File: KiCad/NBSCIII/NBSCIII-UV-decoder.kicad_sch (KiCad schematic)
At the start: 29 parts, among them U2 4053, U3 LM324N

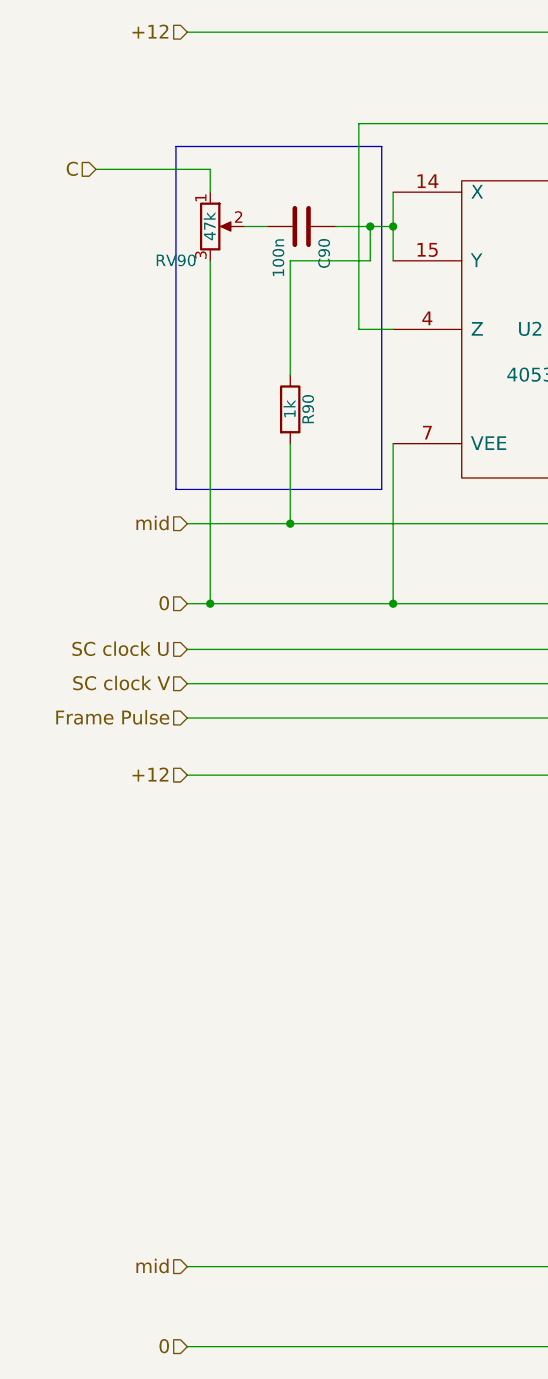
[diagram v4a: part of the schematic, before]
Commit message: Simplify power distribution and make global
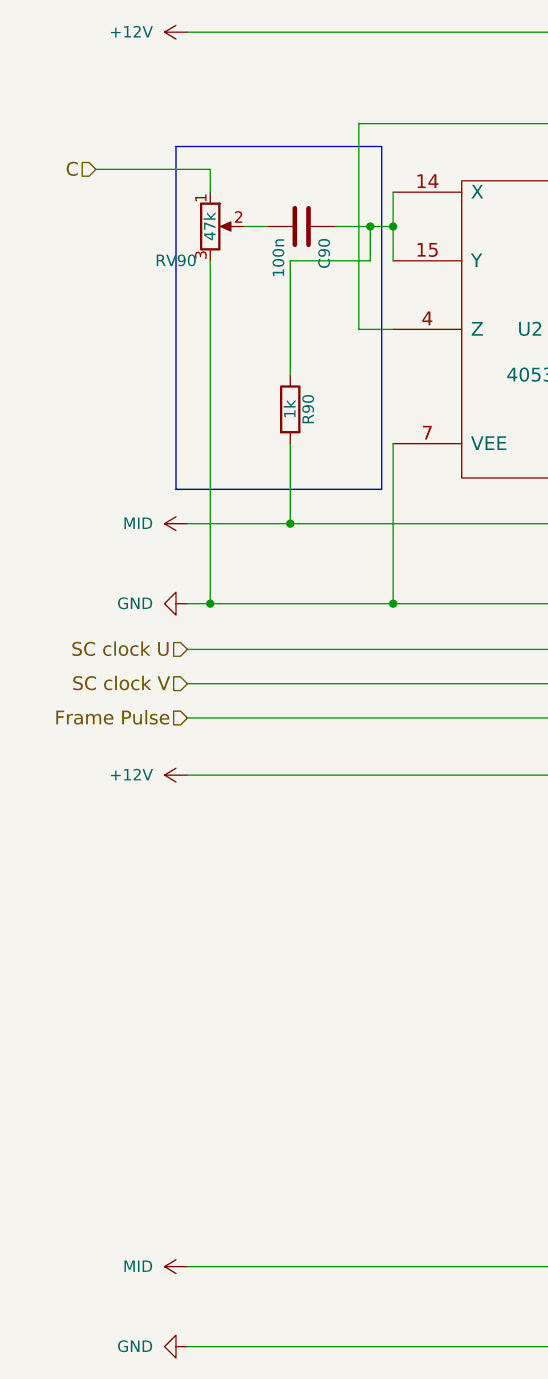
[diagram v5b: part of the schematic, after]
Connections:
- net VDD renamed +12V
- net VSS renamed GND
- net mid renamed MID
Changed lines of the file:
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@@
     (effects (font (size 1.524 1.524)) (justify left))
-  )
-  (hierarchical_label "mid" (shape input) (at 34.29 161.29 180)
-    (effects (font (size 1.524 1.524)) (justify right))
-  )
-  (hierarchical_label "mid" (shape input) (at 34.29 78.74 180)
-    (effects (font (size 1.524 1.524)) (justify right))
-  )
-  (hierarchical_label "+12" (shape input) (at 34.29 24.13 180)
-    (effects (font (size 1.524 1.524)) (justify right))
-  )
-  (hierarchical_label "+12" (shape input) (at 34.29 106.68 180)
-    (effects (font (size 1.524 1.524)) (justify right))
-  )
-  (hierarchical_label "0" (shape input) (at 34.29 87.63 180)
-    (effects (font (size 1.524 1.524)) (justify right))
   )
   (hierarchical_label "SC clock U" (shape input) (at 34.29 92.71 180)
@@
   (hierarchical_label "V" (shape output) (at 236.22 125.73 0)
     (effects (font (size 1.524 1.524)) (justify left))
-  )
-  (hierarchical_label "0" (shape input) (at 34.29 170.18 180)
-    (effects (font (size 1.524 1.524)) (justify right))
   )
   (hierarchical_label "Vburst" (shape output) (at 234.95 34.29 0)
@@
     (pin "2")
   )
+  (symbol (lib_id "power:+12V") (at 34.29 106.68 90) (unit 1)
+    (in_bom yes) (on_board yes) (fields_autoplaced)
+    (property "Reference" "#PWR0107" (id 0) (at 38.1 106.68 0)
+      (effects (font (size 1.27 1.27)) hide)
+    )
+    (property "Value" "+12V" (id 1) (at 30.48 106.6799 90)
+      (effects (font (size 1.27 1.27)) (justify left))
+    )
+    (property "Footprint" "" (id 2) (at 34.29 106.68 0)
+      (effects (font (size 1.27 1.27)) hide)
+    )
+    (property "Datasheet" "" (id 3) (at 34.29 106.68 0)
+      (effects (font (size 1.27 1.27)) hide)
+    )
+    (pin "1")
+  )
+  (symbol (lib_id "NBSCIII:MID") (at 34.29 161.29 90) (unit 1)
+    (in_bom yes) (on_board yes) (fields_autoplaced)
+    (property "Reference" "#PWR0112" (id 0) (at 38.1 161.29 0)
+      (effects (font (size 1.27 1.27)) hide)
+    )
+    (property "Value" "MID" (id 1) (at 30.48 161.2899 90)
+      (effects (font (size 1.27 1.27)) (justify left))
+    )
+    (property "Footprint" "" (id 2) (at 34.29 161.29 0)
+      (effects (font (size 1.27 1.27)) hide)
+    )
+    (property "Datasheet" "" (id 3) (at 34.29 161.29 0)
+      (effects (font (size 1.27 1.27)) hide)
+    )
+    (pin "1")
+  )
+  (symbol (lib_id "power:+12V") (at 34.29 24.13 90) (unit 1)
+    (in_bom yes) (on_board yes) (fields_autoplaced)
+    (property "Reference" "#PWR0110" (id 0) (at 38.1 24.13 0)
+      (effects (font (size 1.27 1.27)) hide)
+    )
+    (property "Value" "+12V" (id 1) (at 30.48 24.1299 90)
+      (effects (font (size 1.27 1.27)) (justify left))
+    )
+    (property "Footprint" "" (id 2) (at 34.29 24.13 0)
+      (effects (font (size 1.27 1.27)) hide)
+    )
+    (property "Datasheet" "" (id 3) (at 34.29 24.13 0)
+      (effects (font (size 1.27 1.27)) hide)
+    )
+    (pin "1")
+  )
+  (symbol (lib_id "power:GND") (at 34.29 170.18 270) (unit 1)
+    (in_bom yes) (on_board yes) (fields_autoplaced)
+    (property "Reference" "#PWR0111" (id 0) (at 27.94 170.18 0)
+      (effects (font (size 1.27 1.27)) hide)
+    )
+    (property "Value" "GND" (id 1) (at 30.48 170.1799 90)
+      (effects (font (size 1.27 1.27)) (justify right))
+    )
+    (property "Footprint" "" (id 2) (at 34.29 170.18 0)
+      (effects (font (size 1.27 1.27)) hide)
+    )
+    (property "Datasheet" "" (id 3) (at 34.29 170.18 0)
+      (effects (font (size 1.27 1.27)) hide)
+    )
+    (pin "1")
+  )
+  (symbol (lib_id "power:GND") (at 34.29 87.63 270) (unit 1)
+    (in_bom yes) (on_board yes) (fields_autoplaced)
+    (property "Reference" "#PWR0108" (id 0) (at 27.94 87.63 0)
+      (effects (font (size 1.27 1.27)) hide)
+    )
+    (property "Value" "GND" (id 1) (at 30.48 87.6299 90)
+      (effects (font (size 1.27 1.27)) (justify right))
+    )
+    (property "Footprint" "" (id 2) (at 34.29 87.63 0)
+      (effects (font (size 1.27 1.27)) hide)
+    )
+    (property "Datasheet" "" (id 3) (at 34.29 87.63 0)
+      (effects (font (size 1.27 1.27)) hide)
+    )
+    (pin "1")
+  )
+  (symbol (lib_id "NBSCIII:MID") (at 34.29 78.74 90) (unit 1)
+    (in_bom yes) (on_board yes) (fields_autoplaced)
+    (property "Reference" "#PWR0109" (id 0) (at 38.1 78.74 0)
+      (effects (font (size 1.27 1.27)) hide)
+    )
+    (property "Value" "MID" (id 1) (at 30.48 78.7399 90)
+      (effects (font (size 1.27 1.27)) (justify left))
+    )
+    (property "Footprint" "" (id 2) (at 34.29 78.74 0)
+      (effects (font (size 1.27 1.27)) hide)
+    )
+    (property "Datasheet" "" (id 3) (at 34.29 78.74 0)
+      (effects (font (size 1.27 1.27)) hide)
+    )
+    (pin "1")
+  )
 )

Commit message: derescue 4053
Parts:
- U2: symbol NBSCIII-rescue:4053 -> 4xxx:4053

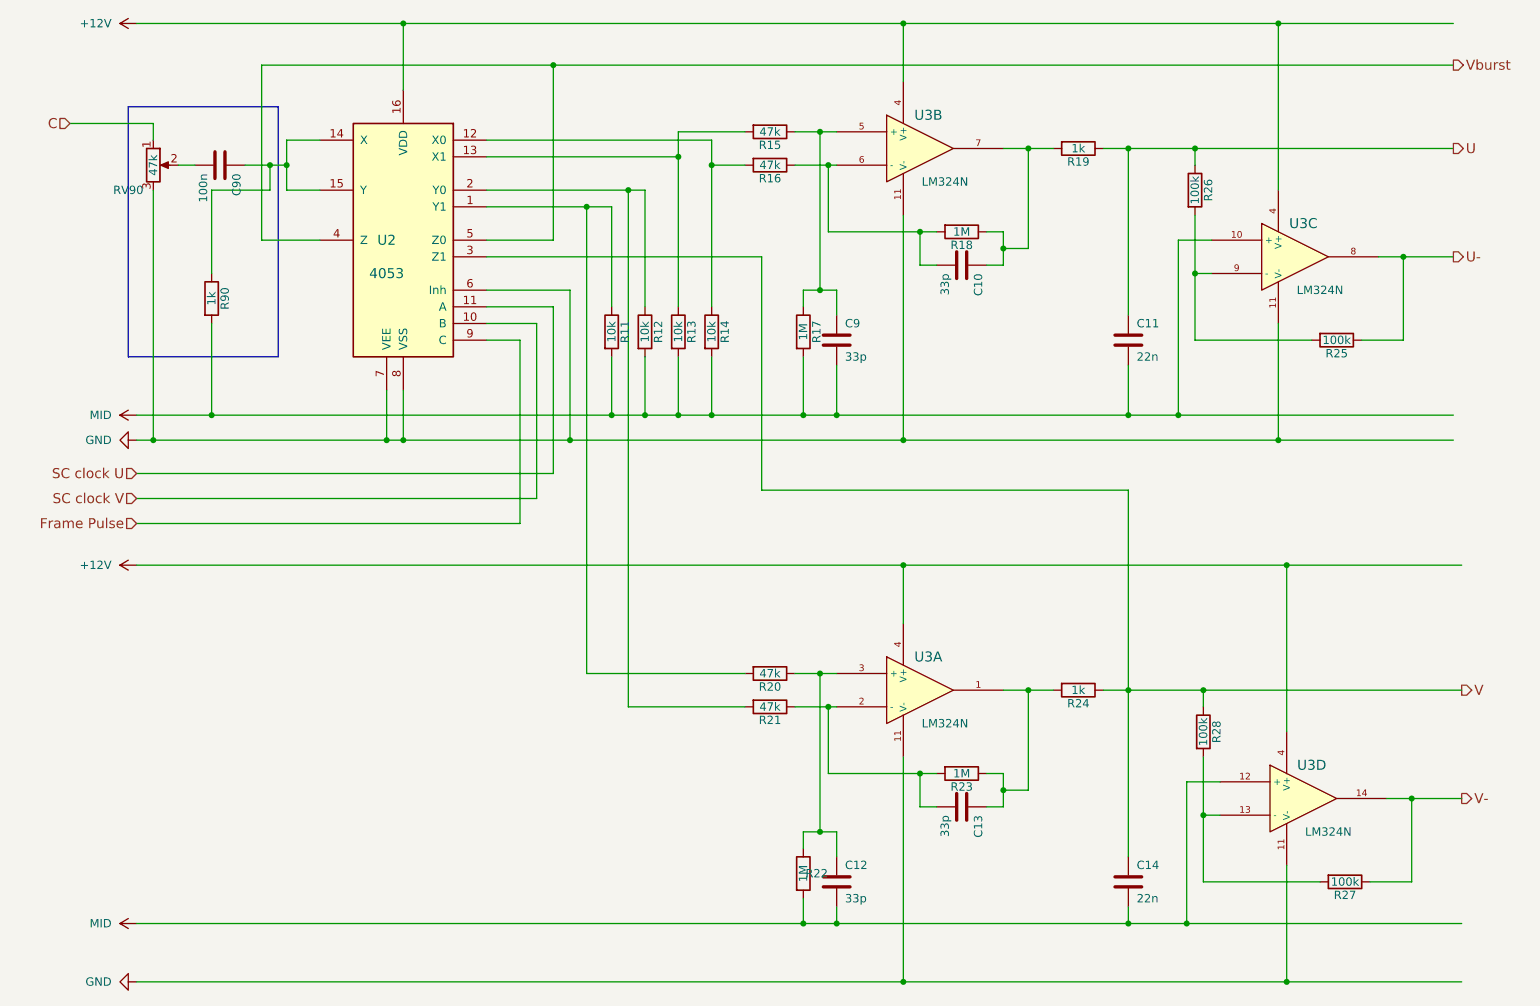
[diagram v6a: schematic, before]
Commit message: derescue lm324
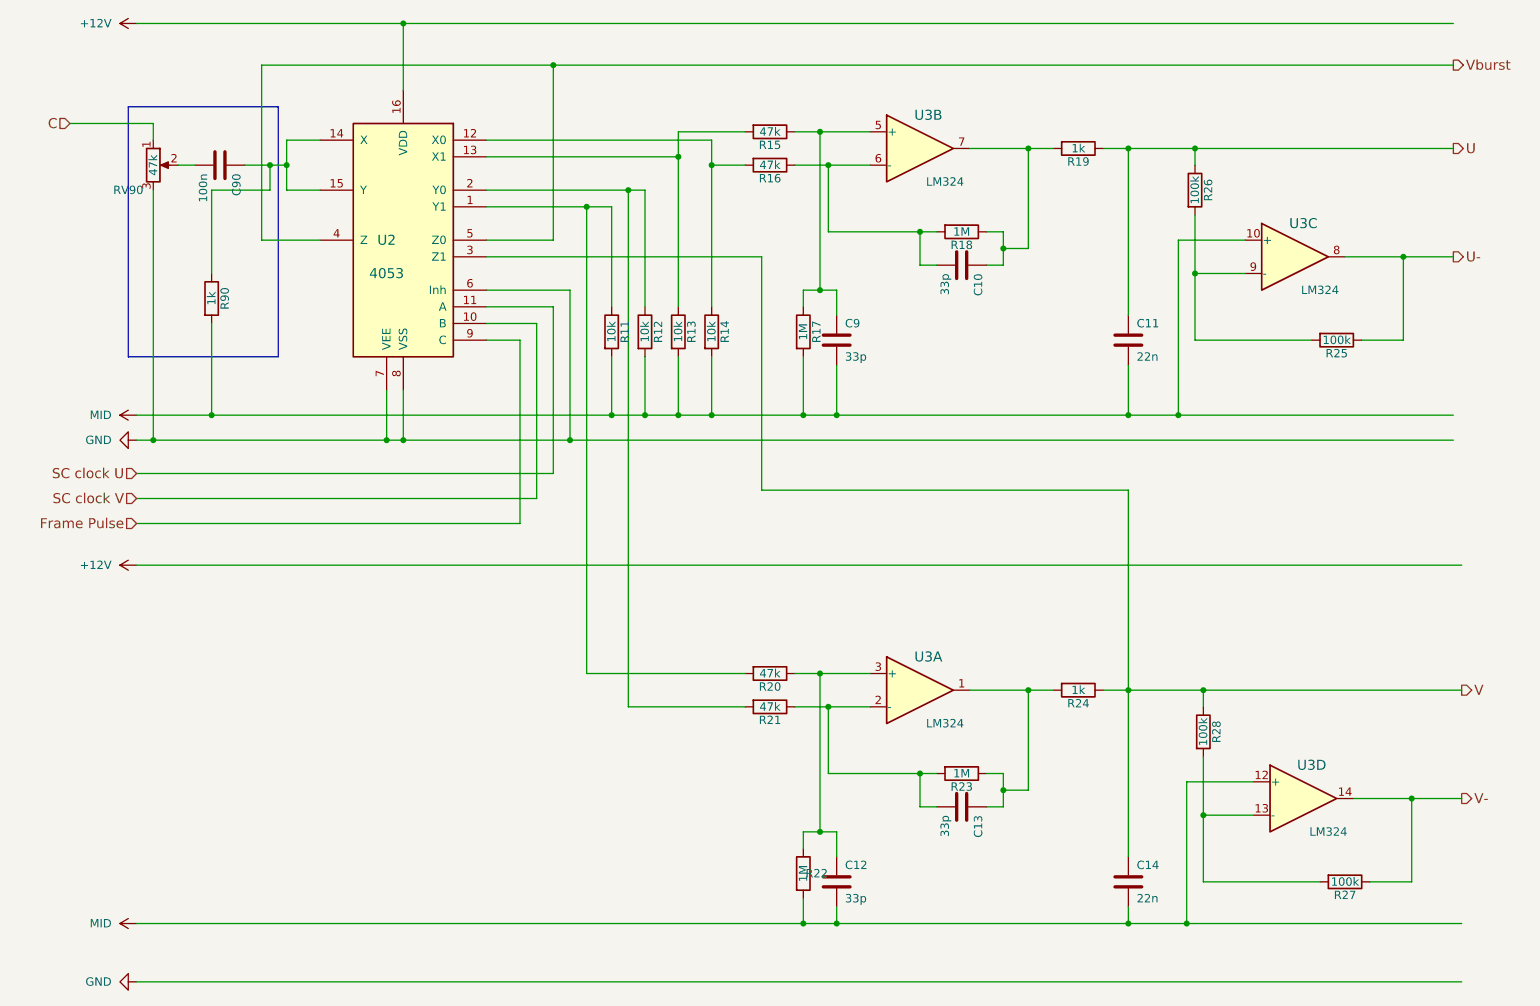
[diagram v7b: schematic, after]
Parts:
- U3: value LM324N -> LM324; symbol NBSCIII-rescue:LM324N -> Amplifier_Operational:LM324
- U3: value LM324N -> LM324; symbol NBSCIII-rescue:LM324 -> Amplifier_Operational:LM324
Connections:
- net +12V: no longer U3.4 (V+), U3.4 (V+), U3.4 (V+), U3.4 (V+)
- net GND: no longer U3.11 (V-), U3.11 (V-), U3.11 (V-), U3.11 (V-)
